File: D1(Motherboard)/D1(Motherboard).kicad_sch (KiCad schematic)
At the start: 69 parts, among them J1 WR-FPC_0.5mm_ZIF_V, J2 USB_C_Receptacle_USB2.0, J3 B2B-PH-K-S, Q1 NX2301P.215, SW1 CHS-02A, U1 ESP32-S2, U2 ICM-20602, U3 WR-FPC_0.5mm_ZIF_H, U4 MIC5353-3.3YMT, U5 FAN5331SX, U6 MCP73831-2-OT, U7 W25Q128JVS, U8 ESP32-S2-MINI-1, Y1 Crystal_GND24

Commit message: Made changed to layout to match available space with S2 Mini 1U
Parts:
- removed C2, C21, C25, C27, C28, C35: 0.1u, Capacitor_SMD:C_0603_1608Metric, symbol Device:C
- removed C30, C32: 1uF, Capacitor_SMD:C_0603_1608Metric, symbol Device:C
- removed C31: 100pF, Capacitor_SMD:C_0603_1608Metric, symbol Device:C
- removed C33, C34, C36, C37: TBD, Capacitor_SMD:C_0603_1608Metric, symbol Device:C
- removed L3: TBD, Inductor_SMD:L_0603_1608Metric, symbol Device:L
- removed R13: 499R, Resistor_SMD:R_0603_1608Metric, symbol Device:R
- removed R14: 10k(NC), Resistor_SMD:R_0603_1608Metric, symbol Device:R
- removed Reference1: Ignion-NN02-101, Ignion_Antenna:NN02-101, symbol Device:Antenna
- removed U1: ESP32-S2, Package_DFN_QFN:QFN-56-1EP_7x7mm_P0.4mm_EP5.6x5.6mm, symbol Espressif:ESP32-S2
- removed U7: W25Q128JVS, Package_SO:SOIC-8_5.23x5.23mm_P1.27mm, symbol Memory_Flash:W25Q128JVS
- removed Y1: Crystal_GND24, Crystal:Crystal_SMD_0603-4Pin_6.0x3.5mm, symbol Device:Crystal_GND24
- U3: value WR-FPC_0.5mm_ZIF_H -> SSD1351
- gave numbers to parts that had none: 2
- renumbered C38 to C21, U8 to U1
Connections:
- net CLK: now also U1.32 (GPIO36)
- net DC: now also U1.12 (GPIO8/ADC1_CH7)
- net Display1_CS: now also U1.13 (GPIO9/ADC1_CH8)
- net Display2_CS: now also U1.14 (GPIO10/ADC1_CH9)
- net Display3_CS: now also U1.15 (GPIO11/ADC2_CH0)
- net Display4_CS: now also U1.16 (GPIO12/ADC2_CH1)
- net Display5_CS: now also U1.17 (GPIO13/ADC2_CH2)
- net Display6_CS: now also U1.18 (GPIO14/ADC2_CH3)
- net INT: now also U1.10 (GPIO6/ADC1_CH5)
- net MISO: now also U1.33 (GPIO37)
- net MOSI: now also U1.31 (GPIO35)
- net RST: now also U1.11 (GPIO7/ADC1_CH6)
- net at R10.2, R11.1: now also U1.5 (GPIO1/ADC1_CH0)
- net U0RXD: no longer names the net of U1.40 (GPIO44/U0RXD/PROG)
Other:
- moved on the sheet: C2, C21, C3, R1, R10, R11, U1

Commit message: More layout work
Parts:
- added D6: GREEN, LED_SMD:LED_0603_1608Metric, symbol Device:LED
- added R12: 1k, Resistor_SMD:R_0603_1608Metric, symbol Device:R
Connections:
- net DC: now also U1.10 (GPIO6/ADC1_CH5); no longer U1.12 (GPIO8/ADC1_CH7)
- net Display1_CS: now also U1.11 (GPIO7/ADC1_CH6); no longer U1.13 (GPIO9/ADC1_CH8)
- net Display2_CS: now also U1.12 (GPIO8/ADC1_CH7); no longer U1.14 (GPIO10/ADC1_CH9)
- net Display3_CS: now also U1.13 (GPIO9/ADC1_CH8); no longer U1.15 (GPIO11/ADC2_CH0)
- net Display4_CS: now also U1.14 (GPIO10/ADC1_CH9); no longer U1.16 (GPIO12/ADC2_CH1)
- net Display5_CS: now also U1.15 (GPIO11/ADC2_CH0); no longer U1.17 (GPIO13/ADC2_CH2)
- net Display6_CS: now also U1.16 (GPIO12/ADC2_CH1); no longer U1.18 (GPIO14/ADC2_CH3)
- net GND: now also D6.1 (K)
- net INT: now also U1.8 (GPIO4/ADC1_CH3); no longer U1.10 (GPIO6/ADC1_CH5)
- net RST: now also U1.9 (GPIO5/ADC1_CH4); no longer U1.11 (GPIO7/ADC1_CH6)
- net at R10.2, R11.1: now also U1.18 (GPIO14/ADC2_CH3); no longer U1.5 (GPIO1/ADC1_CH0)
- new net: R12.1, U1.17 (GPIO13/ADC2_CH2)
- new net: D6.2 (A), R12.2
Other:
- moved on the sheet: R10, R11

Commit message: CHECK SOFTWARE OF MULTIPLE SPI DEVICES FIRST
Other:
- note added: "LOOK AT THIS LINK BEFORE DOING ANYMORE WORK TO FIGURE OUT THE SOFTWARE SIDE OF GETTING MULTIPLE DISPLAYS WORKING AT ONCE https://learn.adafruit.com/animated-snake-eyes-bonnet-for-raspberry-pi/software-installation"
- note removed: "CHECK THE CHIP FOR ESP32 AND THE FOOTPRINT"
- note removed: "FIND VALUES OF CAPS INDUCTORS FOR CRYSTAL AND ANTENNA"
- note removed: "GO THROUGH THE HARDWARE DESIGN GUIDES TO SEE IF ALL ASPECTS ARE VALID"
- note removed: "IS ZERO OHM RESISTOR NEEDED FOR THE CRYSTAL???"
- note removed: "WHAT ARE YOU MEANT TO DO WITH PINS OF ANTENNA?"
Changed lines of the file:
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@@
-    (effects (font (size 5 5) (thickness 1) bold italic) (justify left bottom))
-  )
-  (text "GO THROUGH THE HARDWARE DESIGN GUIDES\nTO SEE IF ALL ASPECTS ARE VALID"
-    (at 422.91 198.12 0)
     (effects (font (size 5 5) (thickness 1) bold italic) (justify left bottom))
   )
@@
     (effects (font (size 5 5) (thickness 1) bold italic) (justify left bottom))
   )
-  (text "WHAT ARE YOU MEANT TO DO WITH PINS OF ANTENNA?" (at 422.91 45.72 0)
+  (text "https://shop.pimoroni.com/products/adafruit-esp32-s2-feather-2-mb-psram-and-stemma-qt-qwiic"
+    (at 2.54 34.29 0)
     (effects (font (size 5 5) (thickness 1) bold italic) (justify left bottom))
   )
-  (text "IS ZERO OHM RESISTOR NEEDED FOR THE CRYSTAL???" (at 422.91 130.81 0)
-    (effects (font (size 5 5) (thickness 1) bold italic) (justify left bottom))
-  )
-  (text "https://shop.pimoroni.com/products/adafruit-esp32-s2-feather-2-mb-psram-and-stemma-qt-qwiic"
-    (at 2.54 34.29 0)
+  (text "LOOK AT THIS LINK BEFORE DOING ANYMORE WORK TO FIGURE OUT THE SOFTWARE SIDE OF GETTING MULTIPLE DISPLAYS WORKING AT ONCE\nhttps://learn.adafruit.com/animated-snake-eyes-bonnet-for-raspberry-pi/software-installation"
+    (at -27.94 133.35 0)
     (effects (font (size 5 5) (thickness 1) bold italic) (justify left bottom))
   )
@@
     (effects (font (size 5 5) (thickness 1) bold italic) (justify left bottom))
   )
-  (text "CHECK THE CHIP FOR ESP32 AND THE FOOTPRINT" (at 421.64 8.89 0)
-    (effects (font (size 5 5) (thickness 1) bold italic) (justify left bottom))
-  )
-  (text "FIND VALUES OF CAPS INDUCTORS FOR CRYSTAL AND ANTENNA"
-    (at 422.91 27.94 0)
-    (effects (font (size 5 5) (thickness 1) bold italic) (justify left bottom))
-  )

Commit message: Some possible links to solutions
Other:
- note added: "TRY OTHER SSD1351 LIBRARIES TO SEE WHAT ELSE YOU CAN DO TO GET MULTIPLE DISPLAYS WORKING"
- note added: "http://adafruit.github.io/Adafruit-SSD1351-library/html/class_adafruit___s_s_d1351.html#ab6e1ac8ed42279367c60977c8bf3fb4f https://github.com/olikraus/ucglib/wiki"
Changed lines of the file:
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@@
+    (effects (font (size 5 5) (thickness 1) bold italic) (justify left bottom))
+  )
+  (text "TRY OTHER SSD1351 LIBRARIES TO SEE WHAT ELSE YOU CAN DO TO GET MULTIPLE DISPLAYS WORKING"
+    (at 10.16 232.41 0)
     (effects (font (size 5 5) (thickness 1) bold italic) (justify left bottom))
   )
@@
     (effects (font (size 5 5) (thickness 1) bold italic) (justify left bottom))
   )
+  (text "http://adafruit.github.io/Adafruit-SSD1351-library/html/class_adafruit___s_s_d1351.html#ab6e1ac8ed42279367c60977c8bf3fb4f\n\nhttps://github.com/olikraus/ucglib/wiki"
+    (at 10.16 255.27 0)
+    (effects (font (size 5 5) (thickness 1) bold italic) (justify left bottom))
+  )

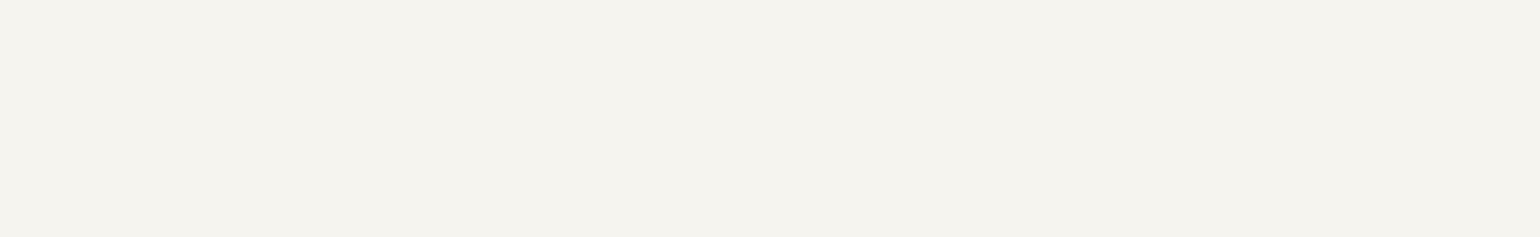
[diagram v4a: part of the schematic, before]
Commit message: Add silkscreen to ESP32
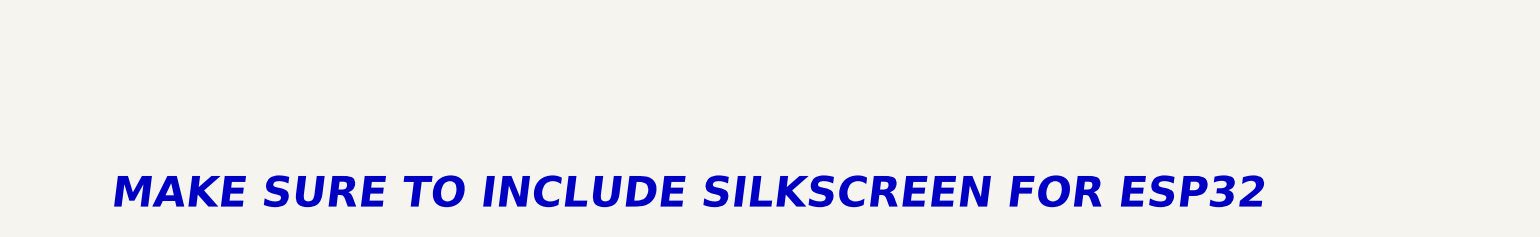
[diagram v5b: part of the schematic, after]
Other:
- note added: "MAKE SURE TO INCLUDE SILKSCREEN FOR ESP32"
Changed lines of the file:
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@@
+    (effects (font (size 5 5) (thickness 1) bold italic) (justify left bottom))
+  )
+  (text "MAKE SURE TO INCLUDE SILKSCREEN FOR ESP32" (at 8.89 290.83 0)
     (effects (font (size 5 5) (thickness 1) bold italic) (justify left bottom))
   )

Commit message: Finished rough layout
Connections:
- net Display1_CS: now also U1.16 (GPIO12/ADC2_CH1); no longer U1.11 (GPIO7/ADC1_CH6)
- net Display2_CS: now also J1.14 (Pin_14), U1.15 (GPIO11/ADC2_CH0); no longer J1.6 (Pin_6), U1.12 (GPIO8/ADC1_CH7)
- net Display3_CS: now also J1.12 (Pin_12), U1.14 (GPIO10/ADC1_CH9); no longer J1.8 (Pin_8), U1.13 (GPIO9/ADC1_CH8)
- net Display4_CS: now also U1.13 (GPIO9/ADC1_CH8); no longer U1.14 (GPIO10/ADC1_CH9)
- net Display5_CS: now also J1.8 (Pin_8), U1.12 (GPIO8/ADC1_CH7); no longer J1.12 (Pin_12), U1.15 (GPIO11/ADC2_CH0)
- net Display6_CS: now also J1.6 (Pin_6), U1.11 (GPIO7/ADC1_CH6); no longer J1.14 (Pin_14), U1.16 (GPIO12/ADC2_CH1)
- net INT: now also U1.9 (GPIO5/ADC1_CH4); no longer U1.8 (GPIO4/ADC1_CH3)
- net Reset: now also J1.4 (Pin_4), U3.21 (RES#)
- removed net RST: J1.4 (Pin_4), U1.9 (GPIO5/ADC1_CH4), U3.21 (RES#)
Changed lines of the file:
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@@
   )
   (text "LOOK AT THIS LINK BEFORE DOING ANYMORE WORK TO FIGURE OUT THE SOFTWARE SIDE OF GETTING MULTIPLE DISPLAYS WORKING AT ONCE\nhttps://learn.adafruit.com/animated-snake-eyes-bonnet-for-raspberry-pi/software-installation"
-    (at -27.94 133.35 0)
+    (at 0 105.41 0)
     (effects (font (size 5 5) (thickness 1) bold italic) (justify left bottom))
   )
@@
     (effects (font (size 5 5) (thickness 1) bold italic) (justify left bottom))
   )
-  (global_label "Display2_CS" (shape input) (at 307.34 125.73 180) (fields_autoplaced)
-    (effects (font (size 1.27 1.27)) (justify right))
-    (property "Intersheet References" "${INTERSHEET_REFS}" (id 0) (at 580.39 233.68 0)
-      (effects (font (size 1.27 1.27)) (justify left) hide)
-    )
-  )
-  (global_label "Display4_CS" (shape input) (at 307.34 130.81 180) (fields_autoplaced)
-    (effects (font (size 1.27 1.27)) (justify right))
-    (property "Intersheet References" "${INTERSHEET_REFS}" (id 0) (at 580.39 233.68 0)
-      (effects (font (size 1.27 1.27)) (justify left) hide)
-    )
-  )
-  (global_label "Display6_CS" (shape input) (at 307.34 135.89 180) (fields_autoplaced)
-    (effects (font (size 1.27 1.27)) (justify right))
-    (property "Intersheet References" "${INTERSHEET_REFS}" (id 0) (at 580.39 236.22 0)
+  (global_label "Display2_CS" (shape input) (at 307.34 133.35 180) (fields_autoplaced)
+    (effects (font (size 1.27 1.27)) (justify right))
+    (property "Intersheet References" "${INTERSHEET_REFS}" (id 0) (at 580.39 25.4 0)
+      (effects (font (size 1.27 1.27)) (justify left) hide)
+    )
+  )
+  (global_label "Display4_CS" (shape input) (at 307.34 128.27 180) (fields_autoplaced)
+    (effects (font (size 1.27 1.27)) (justify right))
+    (property "Intersheet References" "${INTERSHEET_REFS}" (id 0) (at 580.39 25.4 0)
+      (effects (font (size 1.27 1.27)) (justify left) hide)
+    )
+  )
+  (global_label "Display6_CS" (shape input) (at 307.34 123.19 180) (fields_autoplaced)
+    (effects (font (size 1.27 1.27)) (justify right))
+    (property "Intersheet References" "${INTERSHEET_REFS}" (id 0) (at 580.39 22.86 0)
       (effects (font (size 1.27 1.27)) (justify left) hide)
     )
@@
     )
   )
-  (global_label "Display6_CS" (shape input) (at 111.125 143.51 90) (fields_autoplaced)
-    (effects (font (size 1.27 1.27)) (justify left))
-    (property "Intersheet References" "${INTERSHEET_REFS}" (id 0) (at 6.985 40.64 0)
-      (effects (font (size 1.27 1.27)) hide)
+  (global_label "Display6_CS" (shape input) (at 131.445 143.51 90) (fields_autoplaced)
+    (effects (font (size 1.27 1.27)) (justify left))
+    (property "Intersheet References" "${INTERSHEET_REFS}" (id 0) (at 235.585 40.64 0)
+      (effects (font (size 1.27 1.27)) (justify left) hide)
     )
   )
@@
     )
   )
-  (global_label "Display1_CS" (shape input) (at 307.34 123.19 180) (fields_autoplaced)
-    (effects (font (size 1.27 1.27)) (justify right))
-    (property "Intersheet References" "${INTERSHEET_REFS}" (id 0) (at 580.39 251.46 0)
+  (global_label "Display1_CS" (shape input) (at 307.34 135.89 180) (fields_autoplaced)
+    (effects (font (size 1.27 1.27)) (justify right))
+    (property "Intersheet References" "${INTERSHEET_REFS}" (id 0) (at 580.39 7.62 0)
       (effects (font (size 1.27 1.27)) (justify left) hide)
     )
@@
     )
   )
-  (global_label "Display2_CS" (shape input) (at 131.445 143.51 90) (fields_autoplaced)
-    (effects (font (size 1.27 1.27)) (justify left))
-    (property "Intersheet References" "${INTERSHEET_REFS}" (id 0) (at 6.985 40.64 0)
-      (effects (font (size 1.27 1.27)) hide)
+  (global_label "Display2_CS" (shape input) (at 111.125 143.51 90) (fields_autoplaced)
+    (effects (font (size 1.27 1.27)) (justify left))
+    (property "Intersheet References" "${INTERSHEET_REFS}" (id 0) (at 235.585 40.64 0)
+      (effects (font (size 1.27 1.27)) (justify left) hide)
     )
   )
   (global_label "Display4_CS" (shape input) (at 121.285 143.51 90) (fields_autoplaced)
     (effects (font (size 1.27 1.27)) (justify left))
-    (property "Intersheet References" "${INTERSHEET_REFS}" (id 0) (at 6.985 40.64 0)
-      (effects (font (size 1.27 1.27)) hide)
+    (property "Intersheet References" "${INTERSHEET_REFS}" (id 0) (at 235.585 40.64 0)
+      (effects (font (size 1.27 1.27)) (justify left) hide)
     )
   )
@@
     )
   )
-  (global_label "Display5_CS" (shape input) (at 116.205 143.51 90) (fields_autoplaced)
-    (effects (font (size 1.27 1.27)) (justify left))
-    (property "Intersheet References" "${INTERSHEET_REFS}" (id 0) (at 6.985 40.64 0)
-      (effects (font (size 1.27 1.27)) hide)
+  (global_label "Display5_CS" (shape input) (at 126.365 143.51 90) (fields_autoplaced)
+    (effects (font (size 1.27 1.27)) (justify left))
+    (property "Intersheet References" "${INTERSHEET_REFS}" (id 0) (at 235.585 40.64 0)
+      (effects (font (size 1.27 1.27)) (justify left) hide)
     )
   )
@@
     )
   )
-  (global_label "Display3_CS" (shape input) (at 126.365 143.51 90) (fields_autoplaced)
-    (effects (font (size 1.27 1.27)) (justify left))
-    (property "Intersheet References" "${INTERSHEET_REFS}" (id 0) (at 6.985 40.64 0)
-      (effects (font (size 1.27 1.27)) hide)
+  (global_label "Display3_CS" (shape input) (at 116.205 143.51 90) (fields_autoplaced)
+    (effects (font (size 1.27 1.27)) (justify left))
+    (property "Intersheet References" "${INTERSHEET_REFS}" (id 0) (at 235.585 40.64 0)
+      (effects (font (size 1.27 1.27)) (justify left) hide)
     )
   )
@@
     )
   )
-  (global_label "RST" (shape input) (at 200.025 128.27 180) (fields_autoplaced)
-    (effects (font (size 1.27 1.27)) (justify right))
-    (property "Intersheet References" "${INTERSHEET_REFS}" (id 0) (at 6.985 40.64 0)
-      (effects (font (size 1.27 1.27)) hide)
-    )
-  )
-  (global_label "INT" (shape input) (at 307.34 115.57 180) (fields_autoplaced)
-    (effects (font (size 1.27 1.27)) (justify right))
-    (property "Intersheet References" "${INTERSHEET_REFS}" (id 0) (at 580.39 -5.08 0)
+  (global_label "Reset" (shape input) (at 200.025 128.27 180) (fields_autoplaced)
+    (effects (font (size 1.27 1.27)) (justify right))
+    (property "Intersheet References" "${INTERSHEET_REFS}" (id 0) (at 192.4998 128.1906 0)
+      (effects (font (size 1.27 1.27)) (justify right) hide)
+    )
+  )
+  (global_label "INT" (shape input) (at 307.34 118.11 180) (fields_autoplaced)
+    (effects (font (size 1.27 1.27)) (justify right))
+    (property "Intersheet References" "${INTERSHEET_REFS}" (id 0) (at 580.39 -2.54 0)
       (effects (font (size 1.27 1.27)) (justify left) hide)
     )
@@
     )
   )
-  (global_label "Display5_CS" (shape input) (at 307.34 133.35 180) (fields_autoplaced)
-    (effects (font (size 1.27 1.27)) (justify right))
-    (property "Intersheet References" "${INTERSHEET_REFS}" (id 0) (at 580.39 48.26 0)
-      (effects (font (size 1.27 1.27)) hide)
-    )
-  )
-  (global_label "RST" (shape input) (at 136.525 143.51 90) (fields_autoplaced)
-    (effects (font (size 1.27 1.27)) (justify left))
-    (property "Intersheet References" "${INTERSHEET_REFS}" (id 0) (at 6.985 40.64 0)
-      (effects (font (size 1.27 1.27)) hide)
+  (global_label "Display5_CS" (shape input) (at 307.34 125.73 180) (fields_autoplaced)
+    (effects (font (size 1.27 1.27)) (justify right))
+    (property "Intersheet References" "${INTERSHEET_REFS}" (id 0) (at 580.39 210.82 0)
+      (effects (font (size 1.27 1.27)) hide)
+    )
+  )
+  (global_label "Reset" (shape input) (at 136.525 143.51 90) (fields_autoplaced)
+    (effects (font (size 1.27 1.27)) (justify left))
+    (property "Intersheet References" "${INTERSHEET_REFS}" (id 0) (at 136.4456 135.9848 90)
+      (effects (font (size 1.27 1.27)) (justify left) hide)
     )
   )
@@
     )
   )
-  (global_label "Display3_CS" (shape input) (at 307.34 128.27 180) (fields_autoplaced)
-    (effects (font (size 1.27 1.27)) (justify right))
-    (property "Intersheet References" "${INTERSHEET_REFS}" (id 0) (at 580.39 233.68 0)
+  (global_label "Display3_CS" (shape input) (at 307.34 130.81 180) (fields_autoplaced)
+    (effects (font (size 1.27 1.27)) (justify right))
+    (property "Intersheet References" "${INTERSHEET_REFS}" (id 0) (at 580.39 25.4 0)
       (effects (font (size 1.27 1.27)) (justify left) hide)
     )
@@
     )
   )
-  (global_label "RST" (shape input) (at 307.34 118.11 180) (fields_autoplaced)
-    (effects (font (size 1.27 1.27)) (justify right))
-    (property "Intersheet References" "${INTERSHEET_REFS}" (id 0) (at 580.39 35.56 0)
-      (effects (font (size 1.27 1.27)) (justify left) hide)
-    )
-  )

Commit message: Test Commit
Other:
- note added: "https://www.hackster.io/laurentslab/halloween-skull-costume-with-uncanny-eyes-on-esp32-376a13"
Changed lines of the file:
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@@
     (effects (font (size 5 5) (thickness 1) bold italic) (justify left bottom))
   )
-  (text "MAKE SURE TO INCLUDE SILKSCREEN FOR ESP32" (at 8.89 290.83 0)
+  (text "MAKE SURE TO INCLUDE SILKSCREEN FOR ESP32" (at 8.89 271.78 0)
     (effects (font (size 5 5) (thickness 1) bold italic) (justify left bottom))
   )
@@
     (effects (font (size 5 5) (thickness 1) bold italic) (justify left bottom))
   )
+  (text "https://www.hackster.io/laurentslab/halloween-skull-costume-with-uncanny-eyes-on-esp32-376a13"
+    (at 8.89 287.02 0)
+    (effects (font (size 5 5) (thickness 1) bold italic) (justify left bottom))
+  )
